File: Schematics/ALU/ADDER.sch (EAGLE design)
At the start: 44 parts

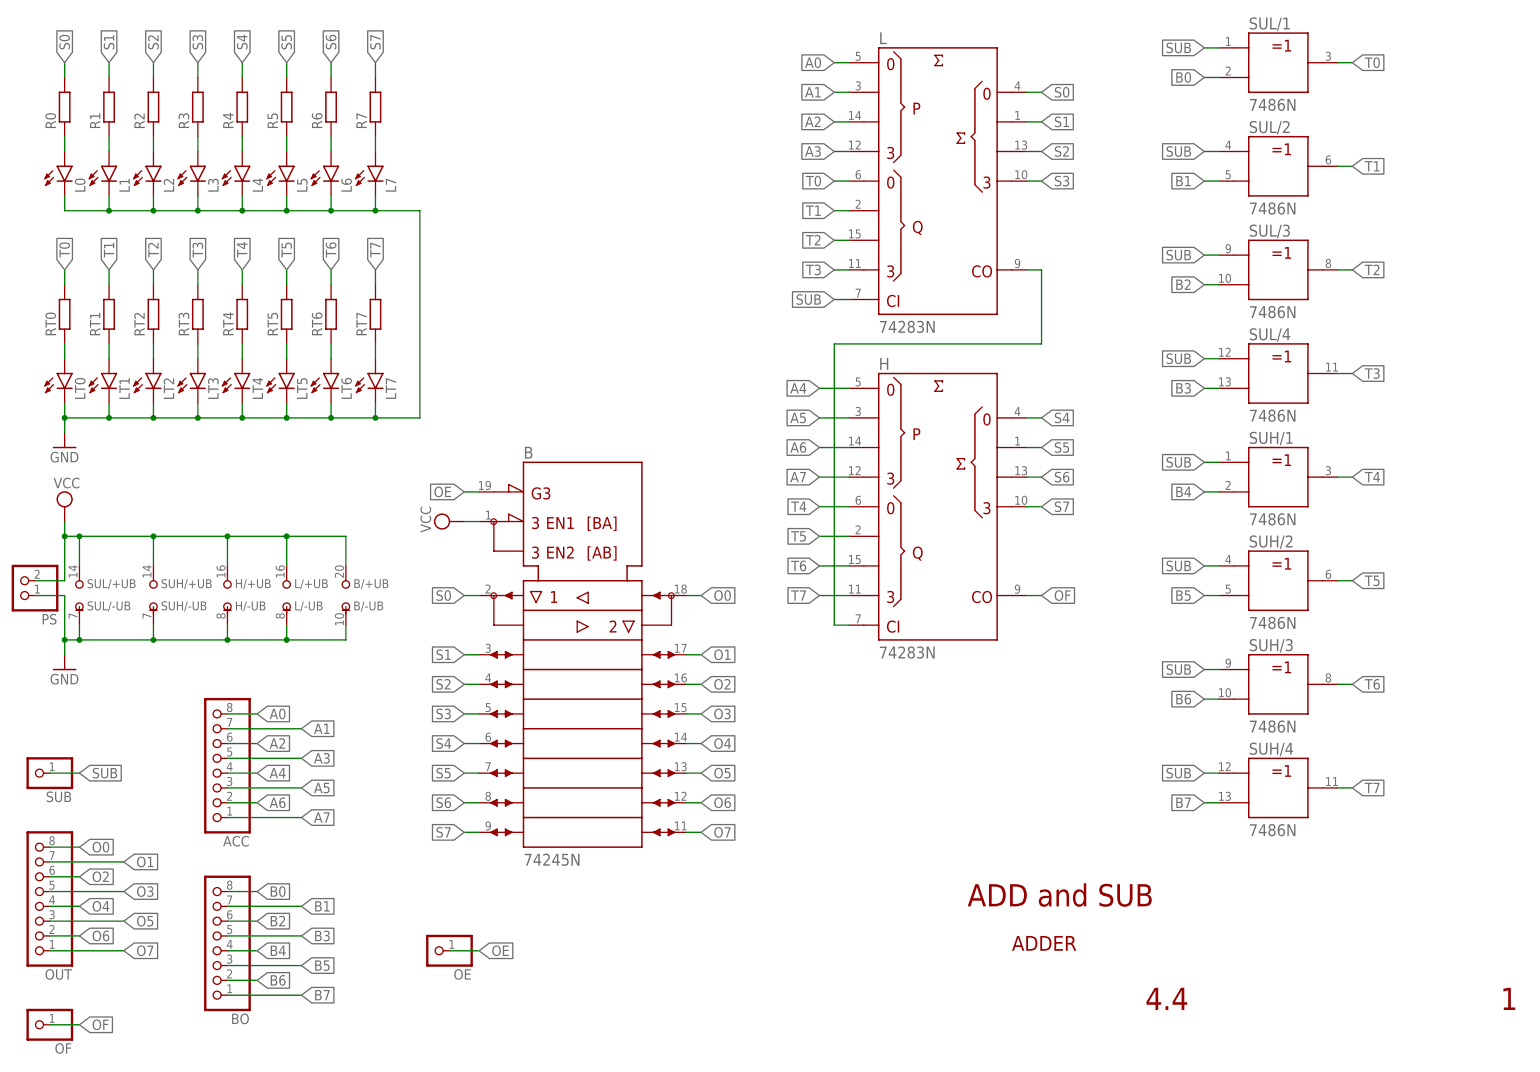
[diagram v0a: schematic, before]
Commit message: Added backbone for ALU.
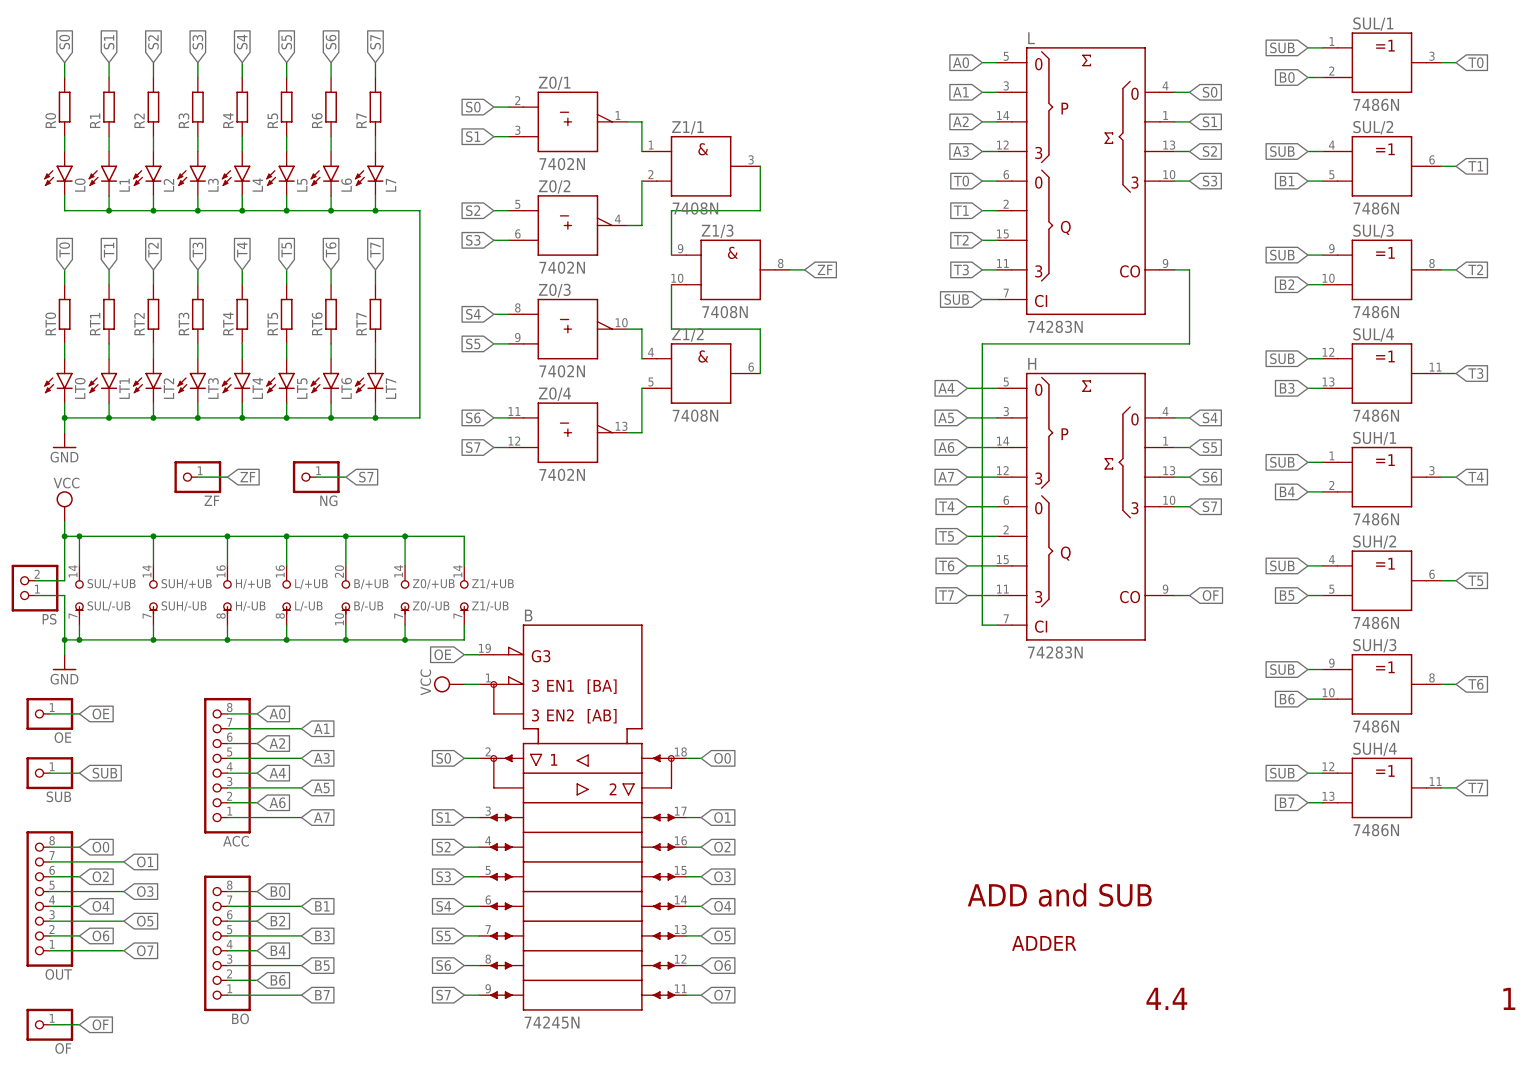
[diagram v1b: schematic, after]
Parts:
- added NG, ZF: (no value), pinhead:PINHD-1X1
- added Z0: 7402N, 74ttl-din:7402N
- added Z1: 7408N, 74ttl-din:7408N
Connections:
- new net N$18: Z0/4.Y, Z1/2.B
- new net N$20: Z0/3.Y, Z1/2.A
- new net N$22: Z1/2.Y, Z1/3.B
- new net N$26: Z1/1.Y, Z1/3.A
- new net N$28: Z0/2.Y, Z1/1.B
- new net N$30: Z0/1.Y, Z1/1.A
- new net ZF: Z1/3.Y, ZF.1
- net GND: now also Z0/-UB.-UB, Z1/-UB.-UB
- net S0: now also Z0/1.A
- net S1: now also Z0/1.B
- net S2: now also Z0/2.A
- net S3: now also Z0/2.B
- net S4: now also Z0/3.A
- net S5: now also Z0/3.B
- net S6: now also Z0/4.A
- net S7: now also NG.1, Z0/4.B
- net VCC: now also Z0/+UB.+UB, Z1/+UB.+UB
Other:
- moved on the sheet: B, H, L, OE, SUH/1, SUH/2, SUH/3, SUH/4, SUL/1, SUL/2, SUL/3, SUL/4
